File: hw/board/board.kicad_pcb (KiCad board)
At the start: 4 copper layers, 100 x 85 mm, 49 parts, among them U1 XC7A35T-FTG256

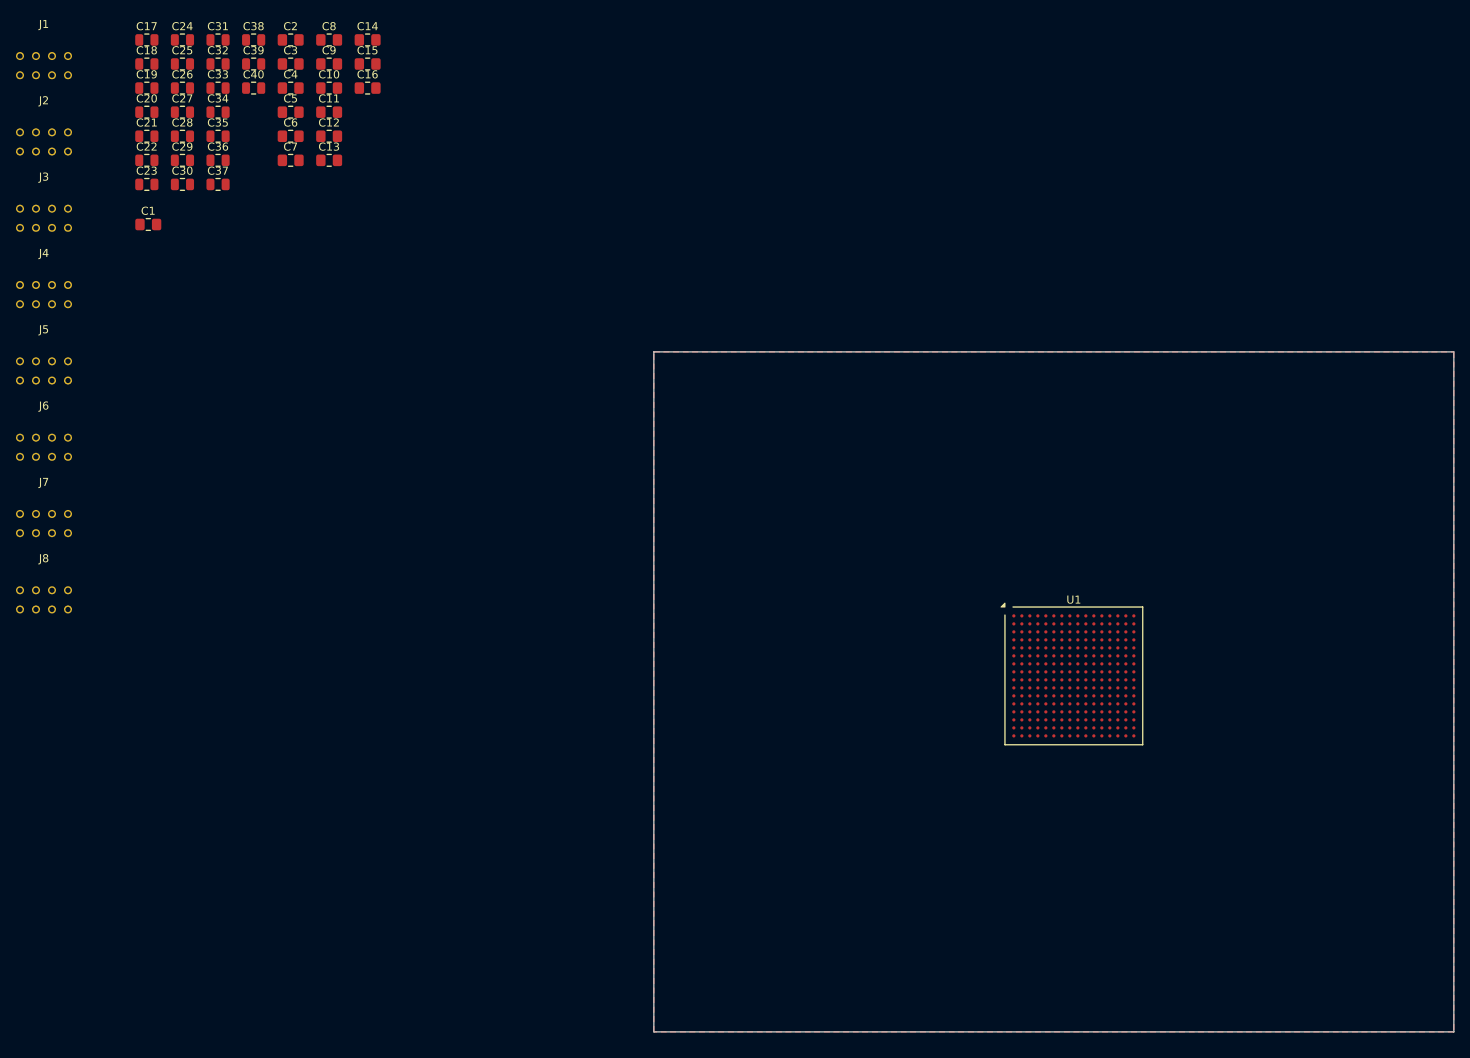
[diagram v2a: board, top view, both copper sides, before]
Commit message: Routed DE-9 connectors
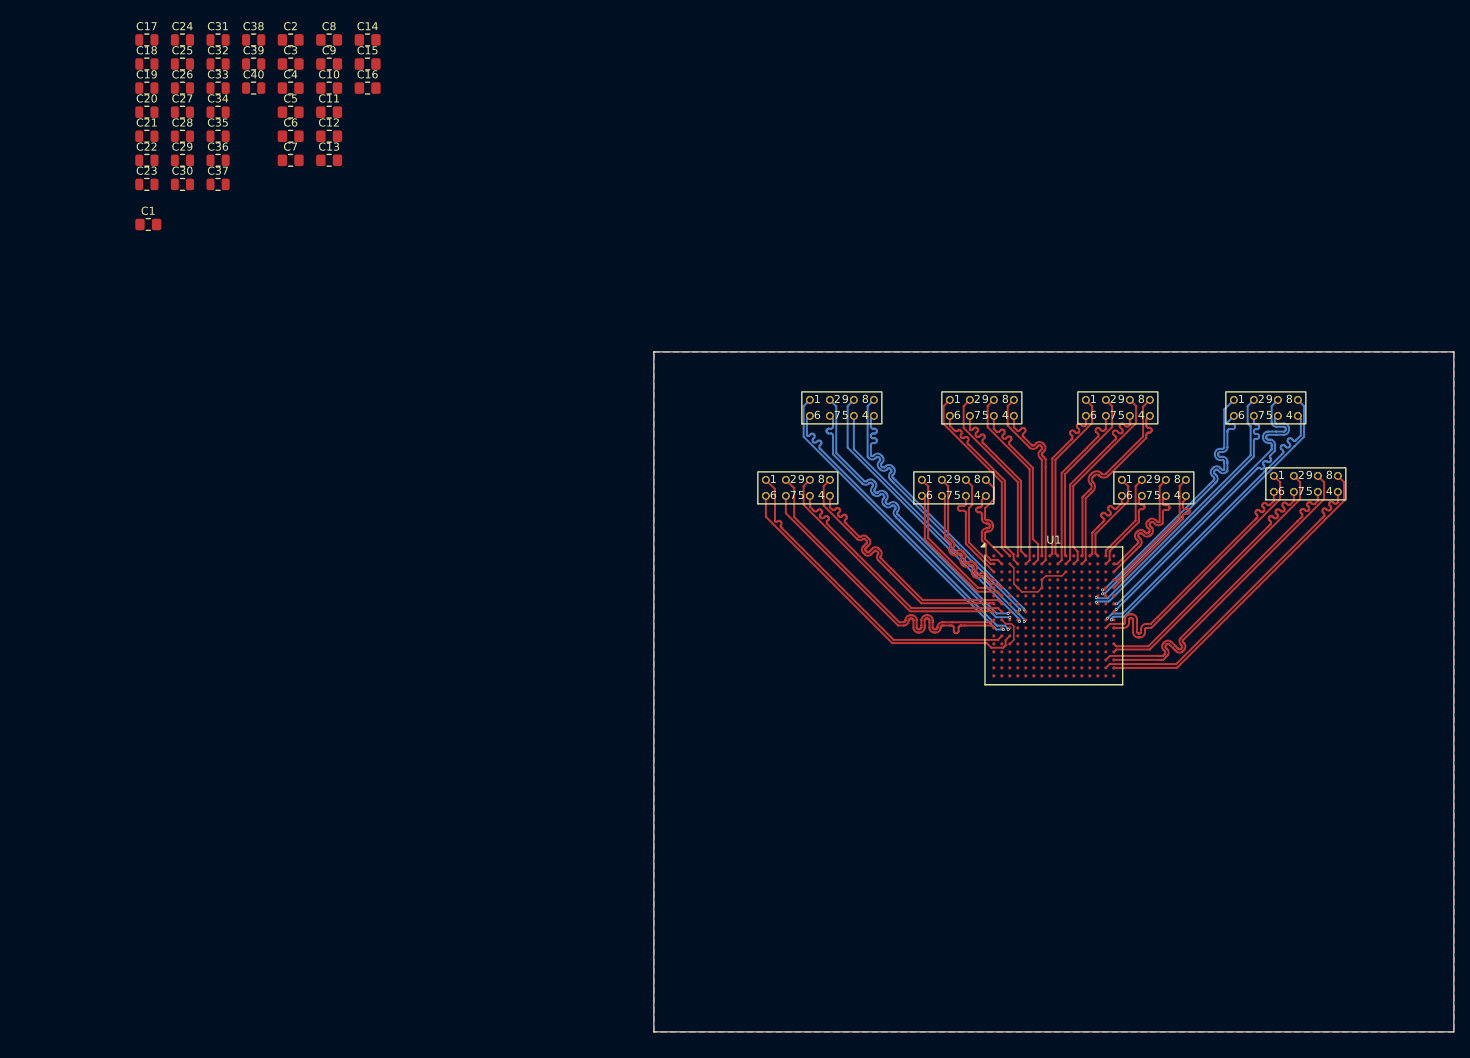
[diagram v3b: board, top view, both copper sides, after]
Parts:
- moved J8 158.4 mm to (165.5, 56.5)
- moved J7 153.4 mm to (160.5, 47.0)
- moved J6 138.8 mm to (146.5, 57.0)
- moved J5 134.3 mm to (142.0, 47.0)
- moved J3 118.6 mm to (121.5, 57.0)
- moved J4 118.1 mm to (125.0, 47.0)
- moved J1 108.6 mm to (107.5, 47.0)
- moved J2 103.7 mm to (102.0, 57.0)
- moved U1 7.91 mm to (134.0, 73.0)
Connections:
- J1 pad 1: unconnected-(J1-D_{in}P-Pad1) -> D_{in}1_P
- J1 pad 2: unconnected-(J1-S_{in}P-Pad2) -> S_{in}1_P
- J1 pad 4: unconnected-(J1-S_{out}N-Pad4) -> S_{out}1_N
- J1 pad 5: unconnected-(J1-D_{out}N-Pad5) -> D_{out}1_N
- J1 pad 6: unconnected-(J1-D_{in}N-Pad6) -> D_{in}1_N
- J1 pad 7: unconnected-(J1-S_{in}N-Pad7) -> S_{in}1_N
- J1 pad 8: unconnected-(J1-S_{out}P-Pad8) -> S_{out}1_P
- J1 pad 9: unconnected-(J1-D_{out}P-Pad9) -> D_{out}1_P
- J2 pad 1: unconnected-(J2-D_{in}P-Pad1) -> D_{in}2_P
- J2 pad 2: unconnected-(J2-S_{in}P-Pad2) -> S_{in}2_P
- J2 pad 4: unconnected-(J2-S_{out}N-Pad4) -> S_{out}2_N
- J2 pad 5: unconnected-(J2-D_{out}N-Pad5) -> D_{out}2_N
- J2 pad 6: unconnected-(J2-D_{in}N-Pad6) -> D_{in}2_N
- J2 pad 7: unconnected-(J2-S_{in}N-Pad7) -> S_{in}2_N
- J2 pad 8: unconnected-(J2-S_{out}P-Pad8) -> S_{out}2_P
- J2 pad 9: unconnected-(J2-D_{out}P-Pad9) -> D_{out}2_P
- J3 pad 1: unconnected-(J3-D_{in}P-Pad1) -> D_{in}3_P
- J3 pad 2: unconnected-(J3-S_{in}P-Pad2) -> S_{in}3_P
- J3 pad 4: unconnected-(J3-S_{out}N-Pad4) -> S_{out}3_N
- J3 pad 5: unconnected-(J3-D_{out}N-Pad5) -> D_{out}3_N
- J3 pad 6: unconnected-(J3-D_{in}N-Pad6) -> D_{in}3_N
- J3 pad 7: unconnected-(J3-S_{in}N-Pad7) -> S_{in}3_N
- J3 pad 8: unconnected-(J3-S_{out}P-Pad8) -> S_{out}3_P
- J3 pad 9: unconnected-(J3-D_{out}P-Pad9) -> D_{out}3_P
- J4 pad 1: unconnected-(J4-D_{in}P-Pad1) -> D_{in}4_P
- J4 pad 2: unconnected-(J4-S_{in}P-Pad2) -> S_{in}4_P
- J4 pad 4: unconnected-(J4-S_{out}N-Pad4) -> S_{out}4_N
- J4 pad 5: unconnected-(J4-D_{out}N-Pad5) -> D_{out}4_N
- J4 pad 6: unconnected-(J4-D_{in}N-Pad6) -> D_{in}4_N
- J4 pad 7: unconnected-(J4-S_{in}N-Pad7) -> S_{in}4_N
- J4 pad 8: unconnected-(J4-S_{out}P-Pad8) -> S_{out}4_P
- J4 pad 9: unconnected-(J4-D_{out}P-Pad9) -> D_{out}4_P
- J5 pad 1: unconnected-(J5-D_{in}P-Pad1) -> D_{in}5_P
- J5 pad 2: unconnected-(J5-S_{in}P-Pad2) -> S_{in}5_P
- J5 pad 4: unconnected-(J5-S_{out}N-Pad4) -> S_{out}5_N
- J5 pad 5: unconnected-(J5-D_{out}N-Pad5) -> D_{out}5_N
- J5 pad 6: unconnected-(J5-D_{in}N-Pad6) -> D_{in}5_N
- J5 pad 7: unconnected-(J5-S_{in}N-Pad7) -> S_{in}5_N
- J5 pad 8: unconnected-(J5-S_{out}P-Pad8) -> S_{out}5_P
- J5 pad 9: unconnected-(J5-D_{out}P-Pad9) -> D_{out}5_P
- J6 pad 1: unconnected-(J6-D_{in}P-Pad1) -> D_{in}6_P
- J6 pad 2: unconnected-(J6-S_{in}P-Pad2) -> S_{in}6_P
- J6 pad 4: unconnected-(J6-S_{out}N-Pad4) -> S_{out}6_N
- J6 pad 5: unconnected-(J6-D_{out}N-Pad5) -> D_{out}6_N
- J6 pad 6: unconnected-(J6-D_{in}N-Pad6) -> D_{in}6_N
- J6 pad 7: unconnected-(J6-S_{in}N-Pad7) -> S_{in}6_N
- J6 pad 8: unconnected-(J6-S_{out}P-Pad8) -> S_{out}6_P
- J6 pad 9: unconnected-(J6-D_{out}P-Pad9) -> D_{out}6_P
- J7 pad 1: unconnected-(J7-D_{in}P-Pad1) -> D_{in}7_P
- J7 pad 2: unconnected-(J7-S_{in}P-Pad2) -> S_{in}7_P
- J7 pad 4: unconnected-(J7-S_{out}N-Pad4) -> S_{out}7_N
- J7 pad 5: unconnected-(J7-D_{out}N-Pad5) -> D_{out}7_N
- J7 pad 6: unconnected-(J7-D_{in}N-Pad6) -> D_{in}7_N
- J7 pad 7: unconnected-(J7-S_{in}N-Pad7) -> S_{in}7_N
- J7 pad 8: unconnected-(J7-S_{out}P-Pad8) -> S_{out}7_P
- J7 pad 9: unconnected-(J7-D_{out}P-Pad9) -> D_{out}7_P
- J8 pad 1: unconnected-(J8-D_{in}P-Pad1) -> D_{in}8_P
- J8 pad 2: unconnected-(J8-S_{in}P-Pad2) -> S_{in}8_P
- J8 pad 4: unconnected-(J8-S_{out}N-Pad4) -> S_{out}8_N
- J8 pad 5: unconnected-(J8-D_{out}N-Pad5) -> D_{out}8_N
- J8 pad 6: unconnected-(J8-D_{in}N-Pad6) -> D_{in}8_N
- J8 pad 7: unconnected-(J8-S_{in}N-Pad7) -> S_{in}8_N
- J8 pad 8: unconnected-(J8-S_{out}P-Pad8) -> S_{out}8_P
- J8 pad 9: unconnected-(J8-D_{out}P-Pad9) -> D_{out}8_P
- U1 pad A10: unconnected-(U1A-IO_L3N_T0_DQS_AD1N_15-PadA10) -> S_{in}5_N
- U1 pad A12: unconnected-(U1A-IO_L5N_T0_AD9N_15-PadA12) -> S_{out}5_N
- U1 pad A13: unconnected-(U1A-IO_L7P_T1_AD2P_15-PadA13) -> D_{in}6_P
- U1 pad A14: unconnected-(U1A-IO_L7N_T1_AD2N_15-PadA14) -> D_{in}6_N
- U1 pad A15: unconnected-(U1A-IO_L9N_T1_DQS_AD3N_15-PadA15) -> S_{in}6_N
- U1 pad A2: unconnected-(U1B-IO_L8N_T1_AD14N_35-PadA2) -> S_{out}3_N
- U1 pad A3: unconnected-(U1B-IO_L4N_T0_35-PadA3) -> D_{in}4_N
- U1 pad A4: unconnected-(U1B-IO_L3N_T0_DQS_AD5N_35-PadA4) -> S_{in}4_N
- U1 pad A5: unconnected-(U1B-IO_L3P_T0_DQS_AD5P_35-PadA5) -> S_{in}4_P
- U1 pad A7: unconnected-(U1B-IO_L1N_T0_AD4N_35-PadA7) -> S_{out}4_N
- U1 pad A8: unconnected-(U1A-IO_L2P_T0_AD8P_15-PadA8) -> D_{in}5_P
- U1 pad A9: unconnected-(U1A-IO_L2N_T0_AD8N_15-PadA9) -> D_{in}5_N
- U1 pad B1: unconnected-(U1B-IO_L9N_T1_DQS_AD7N_35-PadB1) -> D_{out}3_N
- U1 pad B10: unconnected-(U1A-IO_L4P_T0_15-PadB10) -> D_{out}5_P
- U1 pad B11: unconnected-(U1A-IO_L4N_T0_15-PadB11) -> D_{out}5_N
- U1 pad B12: unconnected-(U1A-IO_L5P_T0_AD9P_15-PadB12) -> S_{out}5_P
- U1 pad B15: unconnected-(U1A-IO_L9P_T1_DQS_AD3P_15-PadB15) -> S_{in}6_P
- U1 pad B16: unconnected-(U1A-IO_L10N_T1_AD11N_15-PadB16) -> D_{out}6_N
- U1 pad B2: unconnected-(U1B-IO_L8P_T1_AD14P_35-PadB2) -> S_{out}3_P
- U1 pad B4: unconnected-(U1B-IO_L4P_T0_35-PadB4) -> D_{in}4_P
- U1 pad B5: unconnected-(U1B-IO_L2N_T0_AD12N_35-PadB5) -> D_{out}4_N
- U1 pad B6: unconnected-(U1B-IO_L2P_T0_AD12P_35-PadB6) -> D_{out}4_P
- U1 pad B7: unconnected-(U1B-IO_L1P_T0_AD4P_35-PadB7) -> S_{out}4_P
- U1 pad B9: unconnected-(U1A-IO_L3P_T0_DQS_AD1P_15-PadB9) -> S_{in}5_P
- U1 pad C1: unconnected-(U1B-IO_L9P_T1_DQS_AD7P_35-PadC1) -> D_{out}3_P
- U1 pad C16: unconnected-(U1A-IO_L10P_T1_AD11P_15-PadC16) -> D_{out}6_P
- U1 pad D1: unconnected-(U1B-IO_L10N_T1_AD15N_35-PadD1) -> S_{in}3_N
- U1 pad D16: unconnected-(U1A-IO_L17N_T2_A25_15-PadD16) -> S_{out}6_N
- U1 pad E1: unconnected-(U1B-IO_L15N_T2_DQS_35-PadE1) -> D_{in}3_N
- U1 pad E15: unconnected-(U1A-IO_L18N_T2_A23_15-PadE15) -> D_{in}7_N
- U1 pad E16: unconnected-(U1A-IO_L17P_T2_A26_15-PadE16) -> S_{out}6_P
- U1 pad E2: unconnected-(U1B-IO_L10P_T1_AD15P_35-PadE2) -> S_{in}3_P
- U1 pad F14: unconnected-(U1A-IO_L21N_T3_DQS_A18_15-PadF14) -> S_{in}7_N
- U1 pad F15: unconnected-(U1A-IO_L18P_T2_A24_15-PadF15) -> D_{in}7_P
- U1 pad F2: unconnected-(U1B-IO_L15P_T2_DQS_35-PadF2) -> D_{in}3_P
- U1 pad G1: unconnected-(U1B-IO_L17N_T2_35-PadG1) -> S_{out}2_N
- U1 pad G14: unconnected-(U1A-IO_L21P_T3_DQS_15-PadG14) -> S_{in}7_P
- U1 pad G16: unconnected-(U1A-IO_L22N_T3_A16_15-PadG16) -> D_{out}7_N
- U1 pad G2: unconnected-(U1B-IO_L17P_T2_35-PadG2) -> S_{out}2_P
- U1 pad H1: unconnected-(U1B-IO_L20N_T3_35-PadH1) -> D_{out}2_N
- U1 pad H16: unconnected-(U1A-IO_L22P_T3_A17_15-PadH16) -> D_{out}7_P
- U1 pad H2: unconnected-(U1B-IO_L20P_T3_35-PadH2) -> D_{out}2_P
- U1 pad H3: unconnected-(U1B-IO_L21N_T3_DQS_35-PadH3) -> S_{in}1_N
- U1 pad H4: unconnected-(U1B-IO_L18N_T2_35-PadH4) -> S_{out}1_N
- U1 pad H5: unconnected-(U1B-IO_L18P_T2_35-PadH5) -> S_{out}1_P
- U1 pad J1: unconnected-(U1B-IO_L22N_T3_35-PadJ1) -> S_{in}2_N
- U1 pad J15: unconnected-(U1A-IO_L23P_T3_FOE_B_15-PadJ15) -> S_{out}7_P
- U1 pad J16: unconnected-(U1A-IO_L23N_T3_FWE_B_15-PadJ16) -> S_{out}7_N
- U1 pad J3: unconnected-(U1B-IO_L21P_T3_DQS_35-PadJ3) -> S_{in}1_P
- U1 pad J4: unconnected-(U1B-IO_L19N_T3_VREF_35-PadJ4) -> D_{out}1_N
- U1 pad J5: unconnected-(U1B-IO_L19P_T3_35-PadJ5) -> D_{out}1_P
- U1 pad K1: unconnected-(U1B-IO_L22P_T3_35-PadK1) -> S_{in}2_P
- U1 pad K15: unconnected-(U1A-IO_L2P_T0_D02_14-PadK15) -> D_{in}8_P
- U1 pad K16: unconnected-(U1A-IO_L2N_T0_D03_14-PadK16) -> D_{in}8_N
- U1 pad K2: unconnected-(U1B-IO_L24N_T3_35-PadK2) -> D_{in}1_N
- U1 pad K3: unconnected-(U1B-IO_L24P_T3_35-PadK3) -> D_{in}1_P
- U1 pad L2: unconnected-(U1B-IO_L23N_T3_35-PadL2) -> D_{in}2_N
- U1 pad L3: unconnected-(U1B-IO_L23P_T3_35-PadL3) -> D_{in}2_P
- U1 pad M16: unconnected-(U1A-IO_L7P_T1_D09_14-PadM16) -> S_{in}8_P
- U1 pad N16: unconnected-(U1A-IO_L7N_T1_D10_14-PadN16) -> S_{in}8_N
- U1 pad P15: unconnected-(U1A-IO_L8P_T1_D11_14-PadP15) -> D_{out}8_P
- U1 pad P16: unconnected-(U1A-IO_L8N_T1_D12_14-PadP16) -> D_{out}8_N
- U1 pad R15: unconnected-(U1A-IO_L9P_T1_DQS_14-PadR15) -> S_{out}8_P
- U1 pad R16: unconnected-(U1A-IO_L9N_T1_DQS_D13_14-PadR16) -> S_{out}8_N
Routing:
- net D_{in}2_P: track 0.00 -> 40.9 mm
- net S_{out}8_N: track 0.00 -> 40.9 mm
- net D_{in}2_N: track 0.00 -> 40.8 mm
- net S_{out}8_P: track 0.00 -> 40.8 mm
- net D_{out}8_N: track 0.00 -> 40.8 mm
- net S_{in}2_N: track 0.00 -> 40.7 mm
- net S_{in}2_P: track 0.00 -> 40.7 mm
- net D_{out}8_P: track 0.00 -> 40.7 mm
- net D_{in}1_N: track 0.00 -> 40.2 mm, vias 0 -> 1
- net D_{in}1_P: track 0.00 -> 40.1 mm, vias 0 -> 1
- net S_{in}1_N: track 0.00 -> 40.0 mm, vias 0 -> 1
- net S_{in}1_P: track 0.00 -> 39.9 mm, vias 0 -> 1
- net S_{out}7_N: track 0.00 -> 38.9 mm, vias 0 -> 1
- net S_{out}7_P: track 0.00 -> 38.8 mm, vias 0 -> 1
- net D_{out}7_N: track 0.00 -> 38.8 mm, vias 0 -> 1
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- added copper zone on B.Cu, net GND

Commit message: Began routing decoupling network
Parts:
- C10, C11, C13, C14, C15: moved to B.Cu
- C17, C18, C19, C20, C21, C22, C23, C24, C25, C26, C27, C28: footprint Capacitor_SMD:C_0805_2012Metric -> Capacitor_SMD:C_0805_2012Metric_Pad1.18x1.45mm_HandSolder; moved to B.Cu
- moved C31 137.8 mm to (138.5, 85.3), turned to -90 degrees
- moved C30 136.6 mm to (144.5, 85.3), turned to -90 degrees
- moved C29 136.3 mm to (142.5, 85.3), turned to -90 degrees
- moved C19 135.1 mm to (143.4, 63.4), turned to 90 degrees
- moved C18 134.6 mm to (141.4, 63.4), turned to 90 degrees
- moved C17 134.2 mm to (136.9, 68.1)
- moved C34 134.1 mm to (140.5, 85.3), turned to -90 degrees
- moved C32 132.8 mm to (134.5, 85.3), turned to -90 degrees
- moved C33 132.6 mm to (136.5, 85.3), turned to -90 degrees
- moved C21 129.5 mm to (136.9, 70.1), turned to 180 degrees
- moved C20 128.4 mm to (137.4, 63.4), turned to 90 degrees
- moved C22 127.9 mm to (139.4, 63.4), turned to 90 degrees
- moved C24 125.0 mm to (133.4, 63.4), turned to 90 degrees
- moved C27 122.6 mm to (135.4, 63.4), turned to 90 degrees
- moved C26 120.3 mm to (131.4, 63.4), turned to 90 degrees
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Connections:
- C17 pad 1: +2V5 -> VCCO_15
- C18 pad 1: +2V5 -> VCCO_15
- C19 pad 1: +2V5 -> VCCO_15
- C20 pad 1: +2V5 -> VCCO_15
- C21 pad 1: +2V5 -> VCCO_15
- C22 pad 1: +2V5 -> VCCO_15
- C23 pad 1: +2V5 -> VCCO_35
- C24 pad 1: +2V5 -> VCCO_35
- C25 pad 1: +2V5 -> VCCO_35
- C26 pad 1: +2V5 -> VCCO_35
- C27 pad 1: +2V5 -> VCCO_35
- C28 pad 1: +2V5 -> VCCO_35
- C29 pad 1: +2V5 -> VCCO_14
- C30 pad 1: +2V5 -> VCCO_14
- C31 pad 1: +2V5 -> VCCO_14
- C32 pad 1: +2V5 -> VCCO_14
- C33 pad 1: +2V5 -> VCCO_14
- C34 pad 1: +2V5 -> VCCO_14
- U1 pad A16: +2V5 -> VCCO_15
- U1 pad A6: +2V5 -> VCCO_35
- U1 pad B13: +2V5 -> VCCO_15
- U1 pad B3: +2V5 -> VCCO_35
- U1 pad C10: +2V5 -> VCCO_15
- U1 pad D7: +2V5 -> VCCO_35
- U1 pad E14: +2V5 -> VCCO_15
- U1 pad E4: +2V5 -> VCCO_35
- U1 pad F1: +2V5 -> VCCO_35
- U1 pad H15: +2V5 -> VCCO_15
- U1 pad J12: +2V5 -> VCCO_15
- U1 pad J2: +2V5 -> VCCO_35
- U1 pad L16: +2V5 -> VCCO_14
- U1 pad M13: +2V5 -> VCCO_14
- U1 pad N10: +2V5 -> VCCO_14
- U1 pad P7: +2V5 -> VCCO_14
- U1 pad R14: +2V5 -> VCCO_14
- U1 pad T11: +2V5 -> VCCO_14
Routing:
- net VCCO_14: track 0.00 -> 36.2 mm
- net +2V5: track 15.5 -> 0.00 mm
- net VCCO_35: track 0.00 -> 10.6 mm, vias 0 -> 1
- net +1V0: track 0.00 -> 10.6 mm
- net GND: track 0.00 -> 3.14 mm, vias 0 -> 8
- net D_{in}7_N: track 34.3 -> 33.4 mm
- net D_{in}7_P: track 34.3 -> 33.4 mm
- net D_{in}1_P: track 40.1 -> 40.7 mm
- net D_{in}1_N: track 40.2 -> 40.8 mm
- net VCCO_15: track 0.00 -> 0.42 mm, vias 0 -> 1

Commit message: Added TPS54331 regulator schematic for 2v5 delivery
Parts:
- added C41: 100n, Capacitor_SMD:C_0805_2012Metric_Pad1.18x1.45mm_HandSolder, F.Cu at (166.3, 91.0)
- added C42: 47u, Capacitor_SMD:C_0805_2012Metric_Pad1.18x1.45mm_HandSolder, F.Cu at (166.3, 95.0)
- added C43: 47u, Capacitor_SMD:C_0805_2012Metric_Pad1.18x1.45mm_HandSolder, F.Cu at (166.3, 93.0)
- added C44: 510p, Capacitor_SMD:C_0805_2012Metric, F.Cu at (153.4, 92.6)
- added C45: 47p, Capacitor_SMD:C_0805_2012Metric_Pad1.18x1.45mm_HandSolder, F.Cu at (154.7, 98.0)
- added C46: 10n, Capacitor_SMD:C_0805_2012Metric_Pad1.18x1.45mm_HandSolder, F.Cu at (149.5, 99.0)
- added D1: CD1206, Diode_SMD:D_1206_3216Metric, F.Cu at (166.8, 86.0)
- added L1: 6u8, Inductor_SMD:L_1206_3216Metric, F.Cu at (161.4, 93.3)
- added R1: 41k, Resistor_SMD:R_0805_2012Metric, F.Cu at (155.4, 92.6)
- added R2: 0, Resistor_SMD:R_0805_2012Metric, F.Cu at (159.2, 92.6)
- added R3: 10k, Resistor_SMD:R_0805_2012Metric, F.Cu at (157.3, 92.6)
- added R4: 4k7, Resistor_SMD:R_0805_2012Metric, F.Cu at (151.4, 92.6)
- added R7: 0, Resistor_SMD:R_0805_2012Metric, F.Cu at (144.9, 101.6)
- added U2: TPS54331DR, Snapeda:SOIC127P599X175-8N, F.Cu at (160.6, 99.0)
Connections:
- C1 pad 1: +2V5 -> VCCO_14
- C16 pad 1: +2V5 -> VCCO_14
- C17 pad 1: VCCO_15 -> VCCO_14
- C18 pad 1: VCCO_15 -> VCCO_14
- C19 pad 1: VCCO_15 -> VCCO_14
- C20 pad 1: VCCO_15 -> VCCO_14
- C21 pad 1: VCCO_15 -> VCCO_14
- C22 pad 1: VCCO_15 -> VCCO_14
- C23 pad 1: VCCO_35 -> VCCO_14
- C24 pad 1: VCCO_35 -> VCCO_14
- C25 pad 1: VCCO_35 -> VCCO_14
- C26 pad 1: VCCO_35 -> VCCO_14
- C27 pad 1: VCCO_35 -> VCCO_14
- C28 pad 1: VCCO_35 -> VCCO_14
- C35 pad 1: +2V5 -> VCCO_14
- C36 pad 1: +2V5 -> VCCO_14
- C37 pad 1: +2V5 -> VCCO_14
- C38 pad 1: +2V5 -> VCCO_14
- C39 pad 1: +2V5 -> VCCO_14
- C40 pad 1: +2V5 -> VCCO_14
- U1 pad A16: VCCO_15 -> VCCO_14
- U1 pad A6: VCCO_35 -> VCCO_14
- U1 pad B13: VCCO_15 -> VCCO_14
- U1 pad B3: VCCO_35 -> VCCO_14
- U1 pad C10: VCCO_15 -> VCCO_14
- U1 pad D7: VCCO_35 -> VCCO_14
- U1 pad E14: VCCO_15 -> VCCO_14
- U1 pad E4: VCCO_35 -> VCCO_14
- U1 pad E7: +2V5 -> VCCO_14
- U1 pad F1: VCCO_35 -> VCCO_14
- U1 pad H15: VCCO_15 -> VCCO_14
- U1 pad J12: VCCO_15 -> VCCO_14
- U1 pad J2: VCCO_35 -> VCCO_14
- U1 pad L6: +2V5 -> VCCO_14
- U1 pad M3: +2V5 -> VCCO_14
- U1 pad R4: +2V5 -> VCCO_14
- U1 pad T1: +2V5 -> VCCO_14
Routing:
- net VCCO_14: track 36.2 -> 47.6 mm, vias 0 -> 3
- net VCCO_35: track 10.6 -> 0.00 mm, vias 1 -> 0
- net VCCO_15: track 0.42 -> 0.00 mm, vias 1 -> 0

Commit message: Routed decoupling capacitors
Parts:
- removed C15, C17, C18, C2, C27, C28: 470n, Capacitor_SMD:C_0805_2012Metric_Pad1.18x1.45mm_HandSolder
- removed C29, C30, C38, C39, C40: 470n, Capacitor_SMD:C_0805_2012Metric
- C1, C12, C16, C3, C4, C5, C6, C7, C8, C9: footprint Capacitor_SMD:C_0805_2012Metric_Pad1.18x1.45mm_HandSolder -> Capacitor_SMD:C_0805_2012Metric; moved to B.Cu
- C10, C11, C13, C14, C19, C20, C21, C22, C23, C24, C25, C26, C41, C42, C43, C45, C46: footprint Capacitor_SMD:C_0805_2012Metric_Pad1.18x1.45mm_HandSolder -> Capacitor_SMD:C_0805_2012Metric
- C31, C32, C33, C34, C35, C36, C37: moved to B.Cu
- L1: footprint Inductor_SMD:L_1206_3216Metric -> Inductor_SMD:L_Chilisin_BMRF00101040
- moved C1 124.1 mm to (132.1, 79.0), turned to -90 degrees
- moved C3 121.0 mm to (136.1, 75.6), turned to -90 degrees
- moved C4 120.8 mm to (138.1, 75.6), turned to -90 degrees
- moved C9 120.3 mm to (140.1, 75.6), turned to -90 degrees
- moved C7 119.4 mm to (142.1, 75.6), turned to -90 degrees
- moved C8 117.4 mm to (134.1, 75.6), turned to -90 degrees
- moved C5 116.4 mm to (136.8, 72.5)
- moved C36 115.8 mm to (125.9, 80.3), turned to 180 degrees
- moved C35 115.3 mm to (125.9, 76.3), turned to 180 degrees
- moved C6 113.8 mm to (136.8, 70.5)
- moved C37 113.1 mm to (125.9, 78.3), turned to 180 degrees
- moved C12 104.1 mm to (130.0, 68.5), turned to 180 degrees
- moved R7 21.4 mm to (163.1, 90.5)
- moved L1 15.4 mm to (173.8, 102.5), turned to 180 degrees
- moved C41 13.2 mm to (179.3, 88.5)
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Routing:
- net VCCO_14: track 47.6 -> 19.3 mm, vias 3 -> 4
- net +1V0: track 10.6 -> 7.04 mm
- net GND: track 3.14 -> 2.75 mm, vias 8 -> 3
- added copper zone on B.Cu, net +1V0
- added copper zone on B.Cu, net +1V8
- added copper zone on B.Cu, net VCCO_14
